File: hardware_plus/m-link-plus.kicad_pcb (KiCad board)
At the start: 4 copper layers, 24 x 30 mm, 30 parts, among them J3 SIG, J4 PROGRAM, J5 I2C, SW1 RESTORE SETTINGS, U1 AP1117-33, U2 DRV8837C, U3 DRV8837C, U4 ESP-12F, U5 PCA9685PW, U6 DRV8837C

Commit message: Implement basic support for the Plus version of the hardware.
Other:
- board text added: "DNP"
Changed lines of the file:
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@@
+    (effects (font (size 0.75 0.75) (thickness 0.1875)))
+  )
+  (gr_text "DNP" (at 84.4 75) (layer "F.Fab")
+    (effects (font (size 0.75 0.75) (thickness 0.1875)))
+  )
+  (gr_text "DNP" (at 90.6 74.8) (layer "F.Fab")
+    (effects (font (size 0.75 0.75) (thickness 0.1875)))
+  )
+  (gr_text "DNP" (at 88.2 74.8) (layer "F.Fab")
     (effects (font (size 0.75 0.75) (thickness 0.1875)))
   )

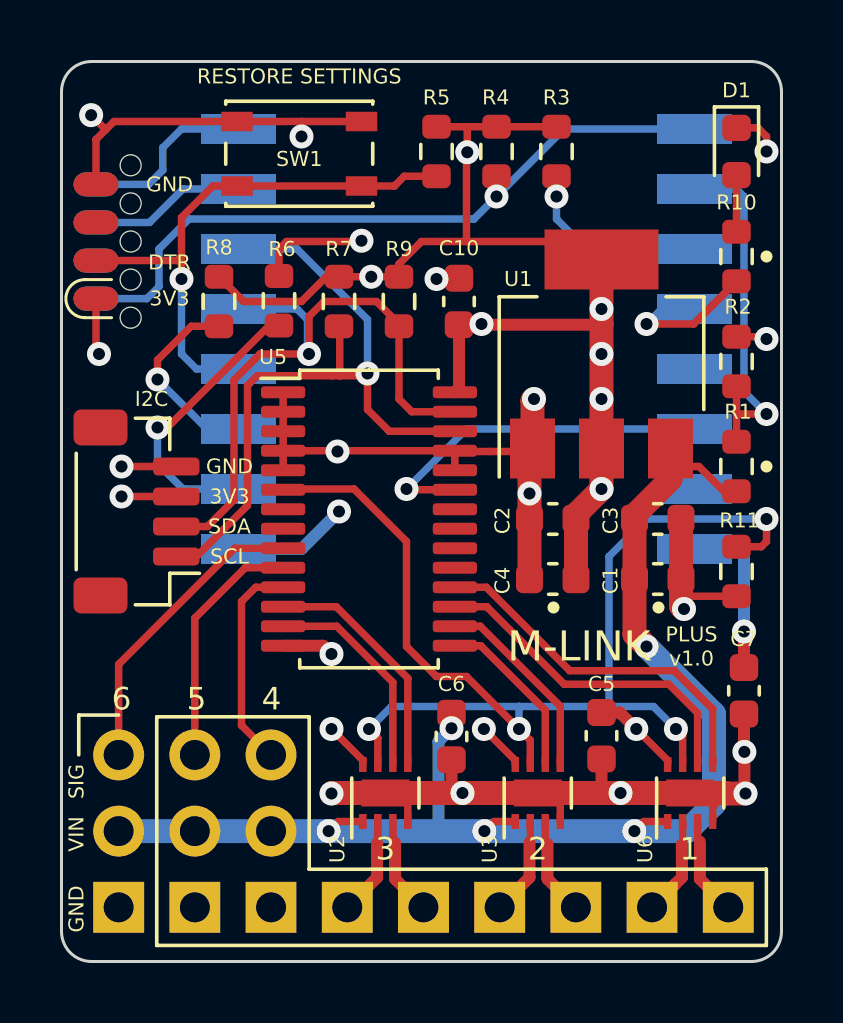
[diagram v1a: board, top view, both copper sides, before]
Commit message: Implement feedback path from PCA9865 to an ESP8266 input for timing.
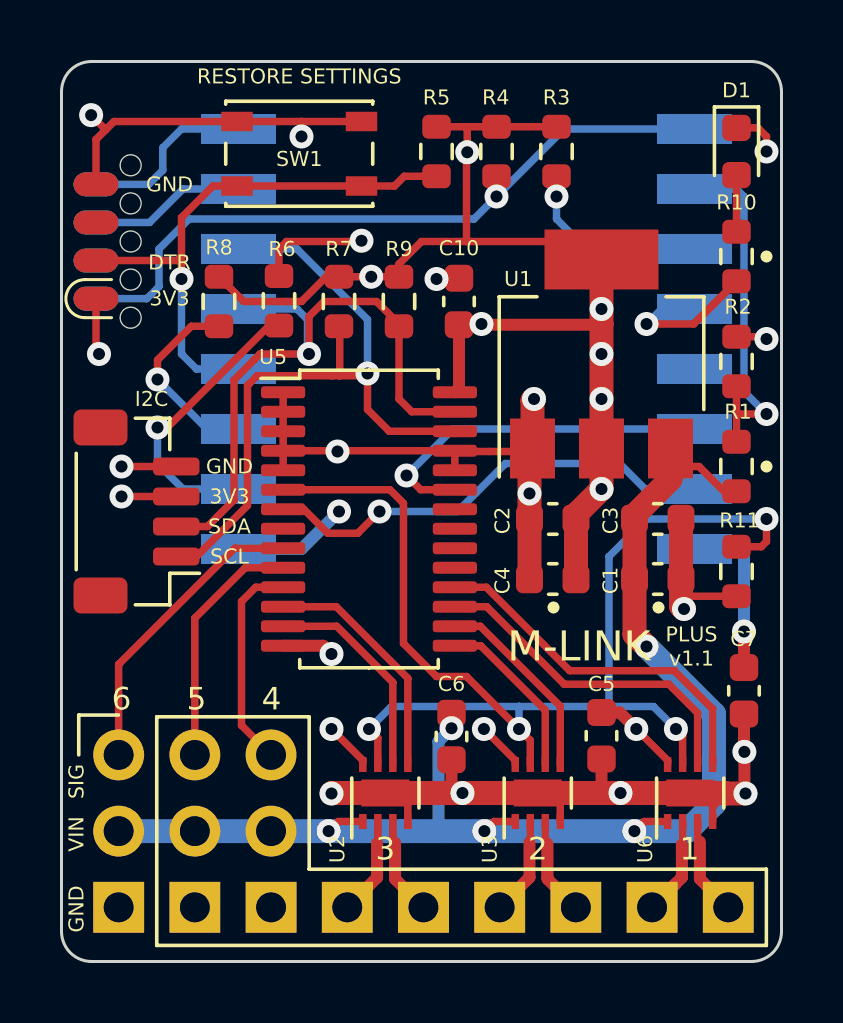
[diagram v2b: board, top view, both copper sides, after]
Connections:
- U4 pad 7: unconnected-(U4-Pad7) -> /FEEDBACK
- U5 pad 7: unconnected-(U5-Pad7) -> /FEEDBACK
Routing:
- net /FEEDBACK: track 0.00 -> 15.4 mm, vias 0 -> 1
- net /SLEEP: track 41.4 -> 42.0 mm
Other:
- board text added: "PLUS v1.1"
- board text removed: "PLUS v1.0"

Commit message: Remove unnecessary resistors and begin improving layout.
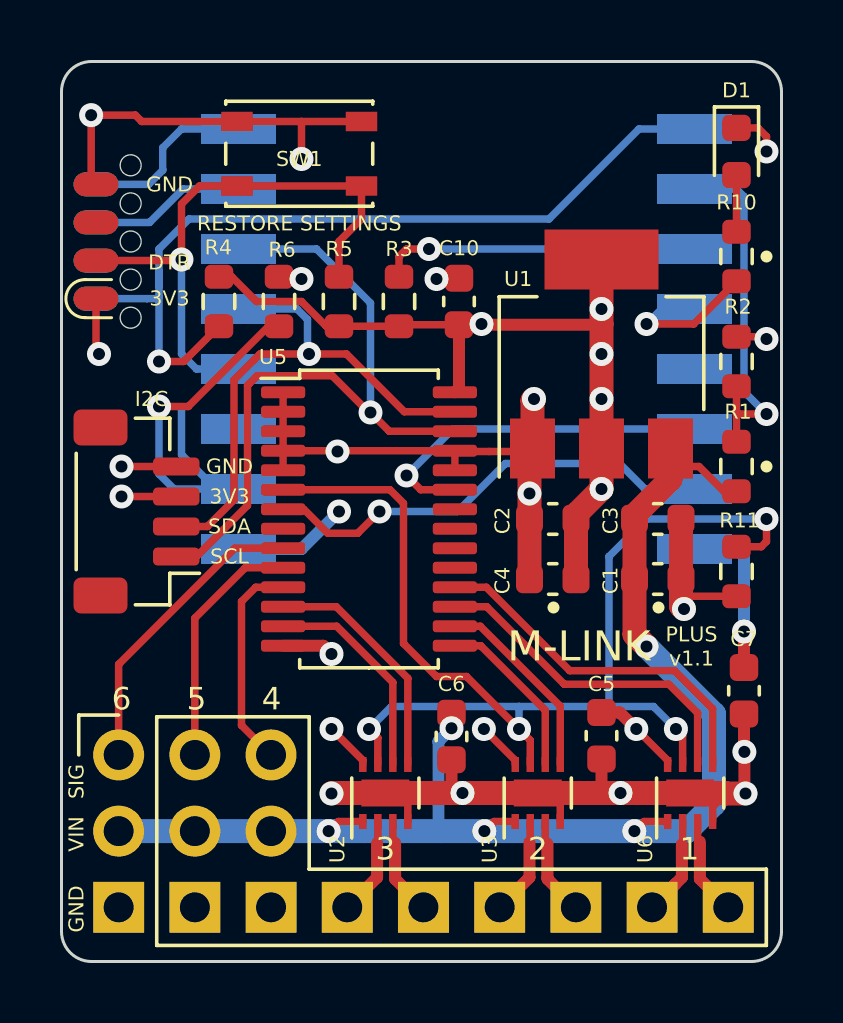
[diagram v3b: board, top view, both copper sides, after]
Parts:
- removed R7, R9: 4k7, Resistor_SMD:R_0603_1608Metric
- removed R8: 10k, Resistor_SMD:R_0603_1608Metric
- moved R4 10.5 mm to (84.2, 77.0)
- moved R3 7.25 mm to (90.2, 77.0), turned to 90 degrees
- moved R5 5.96 mm to (88.2, 77.0), turned to 90 degrees
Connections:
- U4 pad 17: /ESP_LED -> unconnected-(U4-Pad17)
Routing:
- net +3V3: track 56.5 -> 42.9 mm, vias 13 -> 11
- net /ESP_LED: track 6.55 -> 0.00 mm, vias 1 -> 0
- net /RESET: track 23.7 -> 28.4 mm
- net /MTDI: track 9.71 -> 14.2 mm
- net /EN: track 6.44 -> 10.6 mm
- net /SDA: track 21.9 -> 18.3 mm
- net GND: track 88.7 -> 86.8 mm
- net /DTR: track 18.6 -> 19.6 mm
- net /SCL: track 24.4 -> 23.7 mm
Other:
- board text removed: "DNP"

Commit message: Move feedback pin on the pca9685 to be adjacent to the servos.
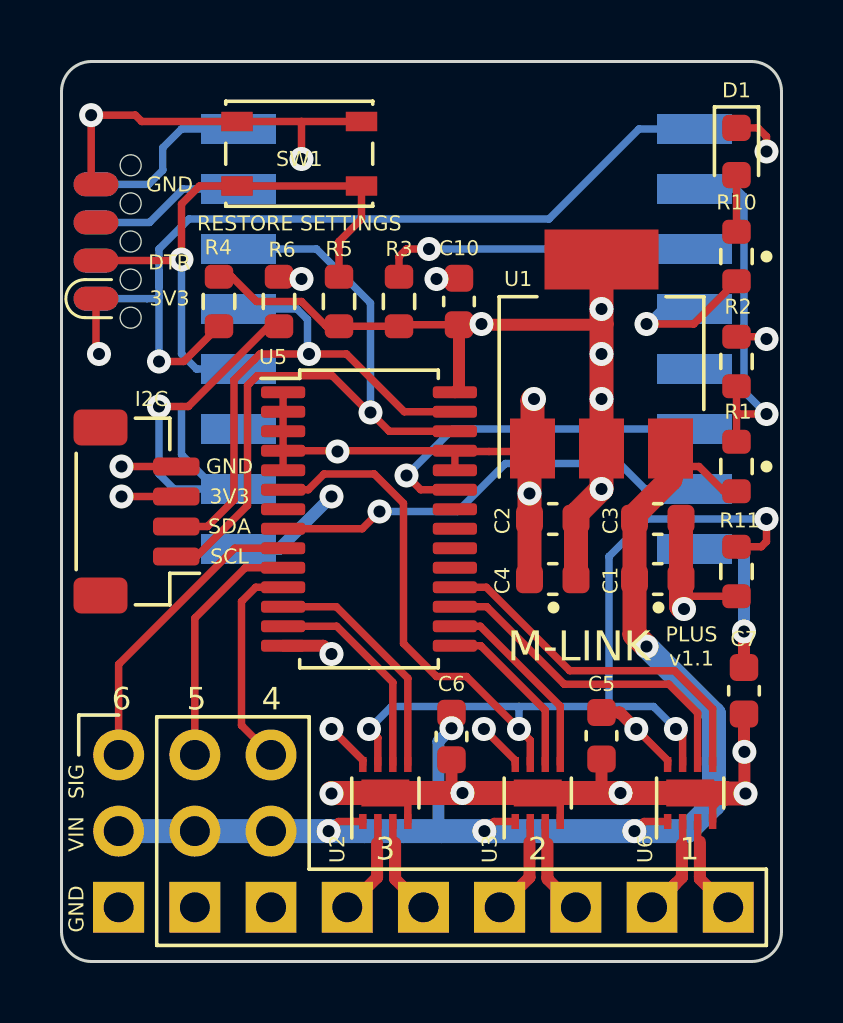
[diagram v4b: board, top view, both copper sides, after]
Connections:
- U5 pad 7: /FEEDBACK -> unconnected-(U5-Pad7)
- U5 pad 8: unconnected-(U5-Pad8) -> /FEEDBACK
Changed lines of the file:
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@@
   (net 26 "unconnected-(J4-Pad3)")
   (net 27 "unconnected-(J4-Pad7)")
-  (net 28 "unconnected-(U5-Pad8)")
+  (net 28 "unconnected-(U5-Pad7)")
   (net 29 "/CH7")
   (net 30 "/M1A")
@@
       (net 21 "/SLEEP") (pinfunction "LED0") (pintype "output"))
     (pad "7" smd roundrect (at -2.8625 -0.325) (size 1.475 0.4) (layers "F.Cu" "F.Paste" "F.Mask") (roundrect_rratio 0.25)
-      (net 40 "/FEEDBACK") (pinfunction "LED1") (pintype "output"))
+      (net 28 "unconnected-(U5-Pad7)") (pinfunction "LED1") (pintype "output+no_connect"))
     (pad "8" smd roundrect (at -2.8625 0.325) (size 1.475 0.4) (layers "F.Cu" "F.Paste" "F.Mask") (roundrect_rratio 0.25)
-      (net 28 "unconnected-(U5-Pad8)") (pinfunction "LED2") (pintype "output+no_connect"))
+      (net 40 "/FEEDBACK") (pinfunction "LED2") (pintype "output"))
     (pad "9" smd roundrect (at -2.8625 0.975) (size 1.475 0.4) (layers "F.Cu" "F.Paste" "F.Mask") (roundrect_rratio 0.25)
       (net 9 "/CH1") (pinfunction "LED3") (pintype "output"))
@@
   (via (at 91.5 76.25) (size 0.8) (drill 0.4) (layers "F.Cu" "B.Cu") (net 1))
   (via (at 99.75 87.25) (size 0.8) (drill 0.4) (layers "F.Cu" "B.Cu") (net 1))
-  (via (at 88.25 84) (size 0.8) (drill 0.4) (layers "F.Cu" "B.Cu") (net 1))
+  (via (at 88 83.5) (size 0.8) (drill 0.4) (layers "F.Cu" "B.Cu") (net 1))
   (via (at 79.987701 70.787701) (size 0.8) (drill 0.4) (layers "F.Cu" "B.Cu") (net 1))
   (via (at 81 82.5) (size 0.8) (drill 0.4) (layers "F.Cu" "B.Cu") (net 1))
@@
   (segment (start 84.794 97.194) (end 85.985 97.194) (width 0.25) (layer "In1.Cu") (net 1))
   (segment (start 80.905 97.194) (end 82.194 97.194) (width 0.25) (layer "In1.Cu") (net 1))
-  (segment (start 87 85.25) (end 88.25 84) (width 0.4) (layer "B.Cu") (net 1))
-  (segment (start 84.9 85.25) (end 87 85.25) (width 0.4) (layer "B.Cu") (net 1))
+  (segment (start 86.25 85.25) (end 88 83.5) (width 0.4) (layer "B.Cu") (net 1))
+  (segment (start 84.9 85.25) (end 86.25 85.25) (width 0.4) (layer "B.Cu") (net 1))
   (segment (start 80.15 75.635) (end 82.865 75.635) (width 0.25) (layer "F.Cu") (net 2))
   (segment (start 84.85 73.15) (end 89 73.15) (width 0.25) (layer "F.Cu") (net 2))
@@
   (segment (start 87.2 77.6) (end 87.2 78.6) (width 0.25) (layer "B.Cu") (net 20))
   (segment (start 86.85 77.25) (end 87.2 77.6) (width 0.25) (layer "B.Cu") (net 20))
-  (segment (start 92.5 89.5) (end 94.25 91.25) (width 0.25) (layer "F.Cu") (net 21))
-  (segment (start 86.3875 83.275) (end 89.949696 83.275) (width 0.25) (layer "F.Cu") (net 21))
+  (segment (start 89.424695 82.75) (end 90.4 83.725305) (width 0.25) (layer "F.Cu") (net 21))
+  (segment (start 87.225 83.275) (end 87.75 82.75) (width 0.25) (layer "F.Cu") (net 21))
+  (segment (start 90.4 88.4) (end 91.5 89.5) (width 0.25) (layer "F.Cu") (net 21))
   (segment (start 99.705 91.4745) (end 99.4805 91.25) (width 0.25) (layer "F.Cu") (net 21))
   (segment (start 101.5 85.175) (end 102.325 85.175) (width 0.25) (layer "F.Cu") (net 21))
   (segment (start 99.705 92.434) (end 99.705 91.4745) (width 0.25) (layer "F.Cu") (net 21))
-  (segment (start 89.949696 83.275) (end 90.4 83.725305) (width 0.25) (layer "F.Cu") (net 21))
+  (segment (start 92.5 89.5) (end 94.25 91.25) (width 0.25) (layer "F.Cu") (net 21))
+  (segment (start 90.4 83.725305) (end 90.4 88.4) (width 0.25) (layer "F.Cu") (net 21))
   (segment (start 89.545 92.434) (end 89.545 91.545) (width 0.25) (layer "F.Cu") (net 21))
   (segment (start 94.625 91.625) (end 94.25 91.25) (width 0.25) (layer "F.Cu") (net 21))
+  (segment (start 86.3875 83.275) (end 87.225 83.275) (width 0.25) (layer "F.Cu") (net 21))
   (segment (start 102.325 85.175) (end 102.5 85) (width 0.25) (layer "F.Cu") (net 21))
   (segment (start 102.5 85) (end 102.5 84.25) (width 0.25) (layer "F.Cu") (net 21))
-  (segment (start 90.4 83.725305) (end 90.4 88.4) (width 0.25) (layer "F.Cu") (net 21))
   (segment (start 91.5 89.5) (end 92.5 89.5) (width 0.25) (layer "F.Cu") (net 21))
   (segment (start 89.545 91.545) (end 89.25 91.25) (width 0.25) (layer "F.Cu") (net 21))
-  (segment (start 90.4 88.4) (end 91.5 89.5) (width 0.25) (layer "F.Cu") (net 21))
   (segment (start 94.625 92.434) (end 94.625 91.625) (width 0.25) (layer "F.Cu") (net 21))
+  (segment (start 87.75 82.75) (end 89.424695 82.75) (width 0.25) (layer "F.Cu") (net 21))
   (via (at 99.4805 91.25) (size 0.8) (drill 0.4) (layers "F.Cu" "B.Cu") (net 21))
   (via (at 94.25 91.25) (size 0.8) (drill 0.4) (layers "F.Cu" "B.Cu") (net 21))
@@
   (segment (start 90.5 82.8) (end 92.05 81.25) (width 0.25) (layer "B.Cu") (net 38))
   (segment (start 100.1 81.25) (end 92.05 81.25) (width 0.25) (layer "B.Cu") (net 38))
-  (segment (start 89.6 84) (end 88.875 84.725) (width 0.25) (layer "F.Cu") (net 40))
-  (segment (start 87.076041 83.925) (end 86.3875 83.925) (width 0.25) (layer "F.Cu") (net 40))
-  (segment (start 88.875 84.725) (end 87.876041 84.725) (width 0.25) (layer "F.Cu") (net 40))
-  (segment (start 87.876041 84.725) (end 87.076041 83.925) (width 0.25) (layer "F.Cu") (net 40))
+  (segment (start 86.3875 84.575) (end 89.025 84.575) (width 0.25) (layer "F.Cu") (net 40))
+  (segment (start 89.025 84.575) (end 89.6 84) (width 0.25) (layer "F.Cu") (net 40))
   (via (at 89.6 84) (size 0.8) (drill 0.4) (layers "F.Cu" "B.Cu") (net 40))
   (segment (start 100.1 83.25) (end 98.45 83.25) (width 0.25) (layer "B.Cu") (net 40))
